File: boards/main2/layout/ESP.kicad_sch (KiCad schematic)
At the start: 16 parts, among them U13 ESP32-S3-MINI-1-N8

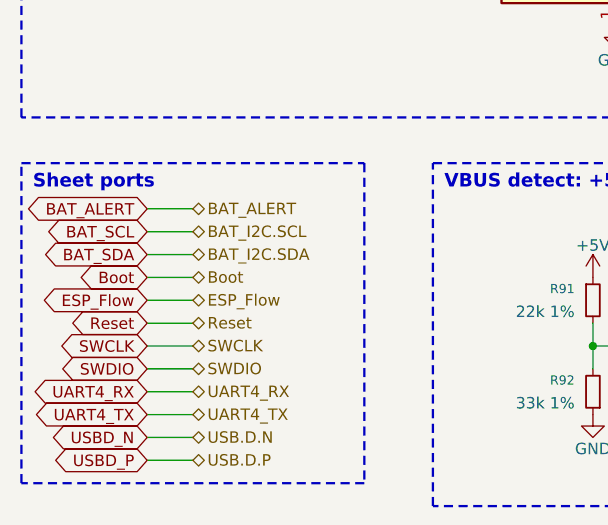
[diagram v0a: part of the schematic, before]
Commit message: 🎨 Place main2's SENSORS sheet, and draw the TLV9001's inputs as + and − in its triangle
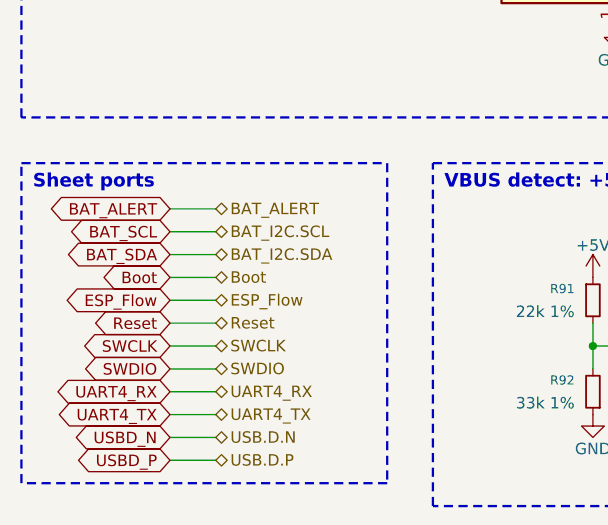
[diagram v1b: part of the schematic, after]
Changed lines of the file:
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@@
 	(wire
 		(pts
-			(xy 26.67 129.54) (xy 31.75 129.54)
+			(xy 29.21 129.54) (xy 34.29 129.54)
 		)
 		(stroke
@@
 	(wire
 		(pts
-			(xy 26.67 132.08) (xy 31.75 132.08)
+			(xy 29.21 132.08) (xy 34.29 132.08)
 		)
 		(stroke
@@
 	(wire
 		(pts
-			(xy 26.67 134.62) (xy 31.75 134.62)
+			(xy 29.21 134.62) (xy 34.29 134.62)
 		)
 		(stroke
@@
 	(wire
 		(pts
-			(xy 26.67 137.16) (xy 31.75 137.16)
+			(xy 29.21 137.16) (xy 34.29 137.16)
 		)
 		(stroke
@@
 	(wire
 		(pts
-			(xy 26.67 139.7) (xy 31.75 139.7)
+			(xy 29.21 139.7) (xy 34.29 139.7)
 		)
 		(stroke
@@
 	(wire
 		(pts
-			(xy 26.67 142.24) (xy 31.75 142.24)
+			(xy 29.21 142.24) (xy 34.29 142.24)
 		)
 		(stroke
@@
 	(wire
 		(pts
-			(xy 26.67 144.78) (xy 31.75 144.78)
+			(xy 29.21 144.78) (xy 34.29 144.78)
 		)
 		(stroke
@@
 	(wire
 		(pts
-			(xy 26.67 147.32) (xy 31.75 147.32)
+			(xy 29.21 147.32) (xy 34.29 147.32)
 		)
 		(stroke
@@
 	(wire
 		(pts
-			(xy 26.67 149.86) (xy 31.75 149.86)
+			(xy 29.21 149.86) (xy 34.29 149.86)
 		)
 		(stroke
@@
 	(wire
 		(pts
-			(xy 26.67 152.4) (xy 31.75 152.4)
+			(xy 29.21 152.4) (xy 34.29 152.4)
 		)
 		(stroke
@@
 	(wire
 		(pts
-			(xy 26.67 154.94) (xy 31.75 154.94)
+			(xy 29.21 154.94) (xy 34.29 154.94)
 		)
 		(stroke
@@
 	(wire
 		(pts
-			(xy 26.67 157.48) (xy 31.75 157.48)
+			(xy 29.21 157.48) (xy 34.29 157.48)
 		)
 		(stroke
@@
 	(global_label "BAT_ALERT"
 		(shape bidirectional)
-		(at 26.67 129.54 180)
-		(effects
-			(font
-				(size 1.27 1.27)
-			)
-			(justify right)
-		)
-		(property "Intersheetrefs" "${INTERSHEET_REFS}"
-			(at 26.67 129.54 0)
+		(at 29.21 129.54 180)
+		(effects
+			(font
+				(size 1.27 1.27)
+			)
+			(justify right)
+		)
+		(property "Intersheetrefs" "${INTERSHEET_REFS}"
+			(at 29.21 129.54 0)
 			(hide yes)
 			(show_name no)
@@
 	(hierarchical_label "BAT_ALERT"
 		(shape bidirectional)
-		(at 31.75 129.54 0)
+		(at 34.29 129.54 0)
 		(effects
 			(font
@@
 	(global_label "BAT_SCL"
 		(shape bidirectional)
-		(at 26.67 132.08 180)
-		(effects
-			(font
-				(size 1.27 1.27)
-			)
-			(justify right)
-		)
-		(property "Intersheetrefs" "${INTERSHEET_REFS}"
-			(at 26.67 132.08 0)
+		(at 29.21 132.08 180)
+		(effects
+			(font
+				(size 1.27 1.27)
+			)
+			(justify right)
+		)
+		(property "Intersheetrefs" "${INTERSHEET_REFS}"
+			(at 29.21 132.08 0)
 			(hide yes)
 			(show_name no)
@@
 	(hierarchical_label "BAT_I2C.SCL"
 		(shape bidirectional)
-		(at 31.75 132.08 0)
+		(at 34.29 132.08 0)
 		(effects
 			(font
@@
 	(global_label "BAT_SDA"
 		(shape bidirectional)
-		(at 26.67 134.62 180)
-		(effects
-			(font
-				(size 1.27 1.27)
-			)
-			(justify right)
-		)
-		(property "Intersheetrefs" "${INTERSHEET_REFS}"
-			(at 26.67 134.62 0)
+		(at 29.21 134.62 180)
+		(effects
+			(font
+				(size 1.27 1.27)
+			)
+			(justify right)
+		)
+		(property "Intersheetrefs" "${INTERSHEET_REFS}"
+			(at 29.21 134.62 0)
 			(hide yes)
 			(show_name no)
@@
 	(hierarchical_label "BAT_I2C.SDA"
 		(shape bidirectional)
-		(at 31.75 134.62 0)
+		(at 34.29 134.62 0)
 		(effects
 			(font
@@
 	(global_label "Boot"
 		(shape bidirectional)
-		(at 26.67 137.16 180)
-		(effects
-			(font
-				(size 1.27 1.27)
-			)
-			(justify right)
-		)
-		(property "Intersheetrefs" "${INTERSHEET_REFS}"
-			(at 26.67 137.16 0)
+		(at 29.21 137.16 180)
+		(effects
+			(font
+				(size 1.27 1.27)
+			)
+			(justify right)
+		)
+		(property "Intersheetrefs" "${INTERSHEET_REFS}"
+			(at 29.21 137.16 0)
 			(hide yes)
 			(show_name no)
@@
 	(hierarchical_label "Boot"
 		(shape bidirectional)
-		(at 31.75 137.16 0)
+		(at 34.29 137.16 0)
 		(effects
 			(font
@@
 	(global_label "ESP_Flow"
 		(shape bidirectional)
-		(at 26.67 139.7 180)
-		(effects
-			(font
-				(size 1.27 1.27)
-			)
-			(justify right)
-		)
-		(property "Intersheetrefs" "${INTERSHEET_REFS}"
-			(at 26.67 139.7 0)
+		(at 29.21 139.7 180)
+		(effects
+			(font
+				(size 1.27 1.27)
+			)
+			(justify right)
+		)
+		(property "Intersheetrefs" "${INTERSHEET_REFS}"
+			(at 29.21 139.7 0)
 			(hide yes)
 			(show_name no)
@@
 	(hierarchical_label "ESP_Flow"
 		(shape bidirectional)
-		(at 31.75 139.7 0)
+		(at 34.29 139.7 0)
 		(effects
 			(font
@@
 	(global_label "Reset"
 		(shape bidirectional)
-		(at 26.67 142.24 180)
-		(effects
-			(font
-				(size 1.27 1.27)
-			)
-			(justify right)
-		)
-		(property "Intersheetrefs" "${INTERSHEET_REFS}"
-			(at 26.67 142.24 0)
+		(at 29.21 142.24 180)
+		(effects
+			(font
+				(size 1.27 1.27)
+			)
+			(justify right)
+		)
+		(property "Intersheetrefs" "${INTERSHEET_REFS}"
+			(at 29.21 142.24 0)
 			(hide yes)
 			(show_name no)
@@
 	(hierarchical_label "Reset"
 		(shape bidirectional)
-		(at 31.75 142.24 0)
+		(at 34.29 142.24 0)
 		(effects
 			(font
@@
 	(global_label "SWCLK"
 		(shape bidirectional)
-		(at 26.67 144.78 180)
-		(effects
-			(font
-				(size 1.27 1.27)
-			)
-			(justify right)
-		)
-		(property "Intersheetrefs" "${INTERSHEET_REFS}"
-			(at 26.67 144.78 0)
+		(at 29.21 144.78 180)
+		(effects
+			(font
+				(size 1.27 1.27)
+			)
+			(justify right)
+		)
+		(property "Intersheetrefs" "${INTERSHEET_REFS}"
+			(at 29.21 144.78 0)
 			(hide yes)
 			(show_name no)
@@
 	(hierarchical_label "SWCLK"
 		(shape bidirectional)
-		(at 31.75 144.78 0)
+		(at 34.29 144.78 0)
 		(effects
 			(font
@@
 	(global_label "SWDIO"
 		(shape bidirectional)
-		(at 26.67 147.32 180)
-		(effects
-			(font
-				(size 1.27 1.27)
-			)
-			(justify right)
-		)
-		(property "Intersheetrefs" "${INTERSHEET_REFS}"
-			(at 26.67 147.32 0)
+		(at 29.21 147.32 180)
+		(effects
+			(font
+				(size 1.27 1.27)
+			)
+			(justify right)
+		)
+		(property "Intersheetrefs" "${INTERSHEET_REFS}"
+			(at 29.21 147.32 0)
 			(hide yes)
 			(show_name no)
@@
 	(hierarchical_label "SWDIO"
 		(shape bidirectional)
-		(at 31.75 147.32 0)
+		(at 34.29 147.32 0)
 		(effects
 			(font
@@
 	(global_label "UART4_RX"
 		(shape bidirectional)
-		(at 26.67 149.86 180)
-		(effects
-			(font
-				(size 1.27 1.27)
-			)
-			(justify right)
-		)
-		(property "Intersheetrefs" "${INTERSHEET_REFS}"
-			(at 26.67 149.86 0)
+		(at 29.21 149.86 180)
+		(effects
+			(font
+				(size 1.27 1.27)
+			)
+			(justify right)
+		)
+		(property "Intersheetrefs" "${INTERSHEET_REFS}"
+			(at 29.21 149.86 0)
 			(hide yes)
 			(show_name no)
@@
 	(hierarchical_label "UART4_RX"
 		(shape bidirectional)
-		(at 31.75 149.86 0)
+		(at 34.29 149.86 0)
 		(effects
 			(font
@@
 	(global_label "UART4_TX"
 		(shape bidirectional)
-		(at 26.67 152.4 180)
-		(effects
-			(font
-				(size 1.27 1.27)
-			)
-			(justify right)
-		)
-		(property "Intersheetrefs" "${INTERSHEET_REFS}"
-			(at 26.67 152.4 0)
+		(at 29.21 152.4 180)
+		(effects
+			(font
+				(size 1.27 1.27)
+			)
+			(justify right)
+		)
+		(property "Intersheetrefs" "${INTERSHEET_REFS}"
+			(at 29.21 152.4 0)
 			(hide yes)
 			(show_name no)
@@
 	(hierarchical_label "UART4_TX"
 		(shape bidirectional)
-		(at 31.75 152.4 0)
+		(at 34.29 152.4 0)
 		(effects
 			(font
@@
 	(global_label "USBD_N"
 		(shape bidirectional)
-		(at 26.67 154.94 180)
-		(effects
-			(font
-				(size 1.27 1.27)
-			)
-			(justify right)
-		)
-		(property "Intersheetrefs" "${INTERSHEET_REFS}"
-			(at 26.67 154.94 0)
+		(at 29.21 154.94 180)
+		(effects
+			(font
+				(size 1.27 1.27)
+			)
+			(justify right)
+		)
+		(property "Intersheetrefs" "${INTERSHEET_REFS}"
+			(at 29.21 154.94 0)
 			(hide yes)
 			(show_name no)
@@
 	(hierarchical_label "USB.D.N"
 		(shape bidirectional)
-		(at 31.75 154.94 0)
+		(at 34.29 154.94 0)
 		(effects
 			(font
@@
 	(global_label "USBD_P"
 		(shape bidirectional)
-		(at 26.67 157.48 180)
-		(effects
-			(font
-				(size 1.27 1.27)
-			)
-			(justify right)
-		)
-		(property "Intersheetrefs" "${INTERSHEET_REFS}"
-			(at 26.67 157.48 0)
+		(at 29.21 157.48 180)
+		(effects
+			(font
+				(size 1.27 1.27)
+			)
+			(justify right)
+		)
+		(property "Intersheetrefs" "${INTERSHEET_REFS}"
+			(at 29.21 157.48 0)
 			(hide yes)
 			(show_name no)
@@
 	(hierarchical_label "USB.D.P"
 		(shape bidirectional)
-		(at 31.75 157.48 0)
+		(at 34.29 157.48 0)
 		(effects
 			(font
@@
 	(rectangle
 		(start 12.7 124.46)
-		(end 50.8 160.02)
+		(end 53.34 160.02)
 		(stroke
 			(width 0.254)

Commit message: 🚧 Place and route main2 but for 12 connections
place.py places every part and route.py pours the planes and routes the board, with hand-routed
fixes on top. 12 connections are still open (boards/main2/layout/README.md, Layout), so DRC and
the layout check fail on them; every other gate passes.
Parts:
- removed R87: 1k 1%, stdlib_kicad-footprints_Resistor_SMD:R_0402_1005Metric, symbol R_Small
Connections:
- net ESP.ESP_BOOT0: no longer names the net of U13.18 (IO14)
- no-connect marks 25 -> 26
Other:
- note added: "Links to the MCU: SWCLK, UART4"
- note removed: "Links to the MCU: SWCLK, BOOT0, UART4"
- moved on the sheet: R88

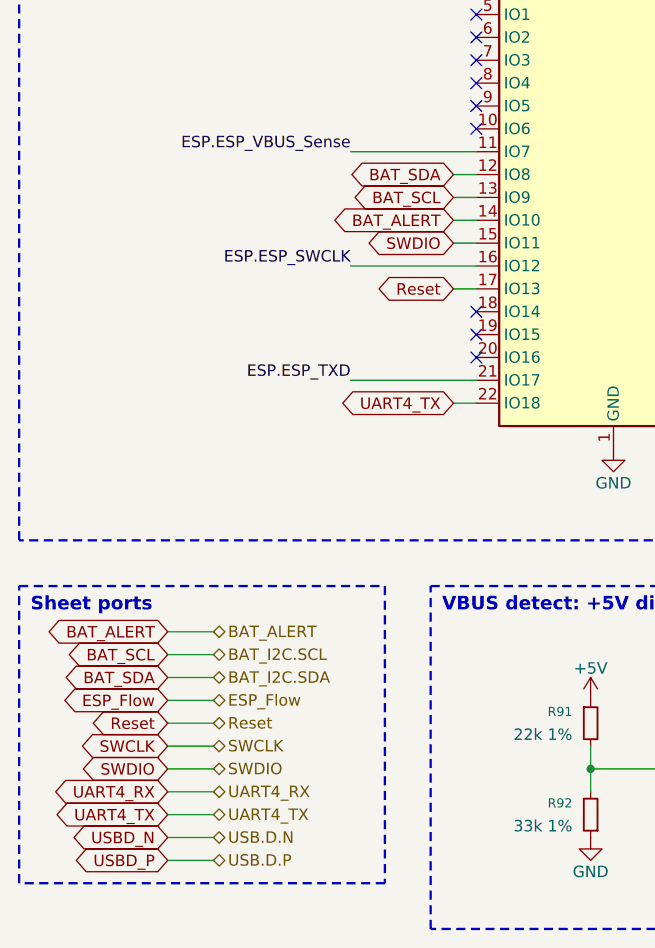
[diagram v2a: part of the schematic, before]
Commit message: ✨ Route main2 completely and fuse its battery input
- Every connection routed: short In2.Cu hops for digital STM32/ESP32 lines (never under
  switching or analog B.Cu copper, off the VBAT pour, out of the STM32 islands, In2 ground
  kept one plane), checked by a new layout test; F.Cu/B.Cu ground pours, ground stitching
  vias and teardrops.
- ADC pins swapped for the routing: Current_Sensor_Left on PB1 (fast channel), Wall_Sensor_0
  on PA4, Wall_Sensor_3 on PC0; firmware changes updated.
- Battery fuse F1 (Littelfuse 0501020.WR1, 20 A, 150 A at 32 VDC) from J1 to VBAT, the TVS and
  the switch drive behind it; the INA228 battery monitor and its shunt removed.
- route.py's DRC refills zones in KiCad, as the DRC gate does.
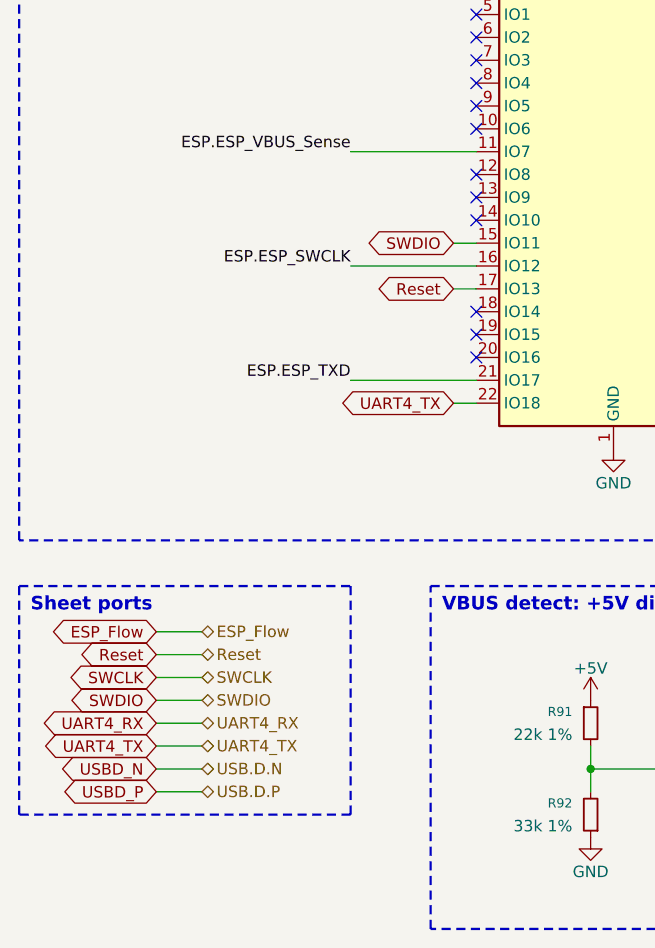
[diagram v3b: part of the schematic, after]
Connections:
- net BAT_ALERT: no longer names the net of U13.14 (IO10)
- net BAT_SCL: no longer names the net of U13.13 (IO9)
- net BAT_SDA: no longer names the net of U13.12 (IO8)
- no-connect marks 26 -> 29

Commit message: 🐛 Fix main2's review findings and settle its open doubts
Schematic and parts:
- Battery input: F1 is a 12 A Littelfuse 501 (0501012.WR1). C58 now sits
  gate-source with C114 gate-drain, so Q6 stays off at plug-in. D16 clamps
  Q8's VGS. R44/R45 are 10k/2k, so VBAT can't float up on USB alone.
- Capacitors: VBAT and VSYS use 1210/0805 50 V parts, sized with Samsung's
  DC-bias curves. C109 is fitted.
- Drivers: R66/R76 are removed (the chokes are needed). ITRIP and the fan
  limit are retuned. The INA241 R_iso is 150 Ohm.
- Rails are declared as ranges, and the abs-max checks run under the TVS
  clamp.
- STM32 pin swaps for routing: the wall selectors move to TIM3,
  Motor_Left_EN to TIM8_CH2 and LED_ARGB to TIM17. CubeMX 6.18.1 confirms
  the map.
- firmware_changes.toml registers the matching firmware changes: the ADC
  0.7 us sampling time, the TIM4-triggered DAC, the fan's 50 kHz start, a
  wheel-sign self-check, VDDA tracking, contest mode, the debug halt and
  others.

Layout:
- USB D+/D- are routed as a coupled pair. The track floor is 0.12 mm.
- Stubs and detours are trimmed. The In2 VCORE/3V3_D islands are shrunk.
- The board is notched under the ESP32 antenna.
- Ground stitching, thermal reliefs, open thermal vias with split paste,
  DRV8874 heat islands and teardrops are added.
- 11 joins remain for hand-routing (layout README, Open items).

Doubts are closed by datasheets, vendor SPICE models and new research
calculations instead of bench TODOs. Tests cover each review item.
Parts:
- C109: now fitted
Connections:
- net ESP_Flow: now also U13.17 (IO13); no longer U13.25 (IO21)
- net Reset: now also U13.25 (IO21); no longer U13.17 (IO13)
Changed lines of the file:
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@@
 		(on_board yes)
 		(in_pos_files yes)
-		(dnp yes)
+		(dnp no)
 		(property "Reference" "C109"
 			(at 142.494 31.75 0)
@@
 		)
 	)
-	(global_label "Reset"
+	(global_label "ESP_Flow"
 		(shape bidirectional)
 		(at 60.96 91.44 180)
@@
 		)
 	)
-	(global_label "ESP_Flow"
+	(global_label "Reset"
 		(shape bidirectional)
 		(at 96.52 66.04 0)
